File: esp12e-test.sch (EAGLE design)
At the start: 15 parts, among them IC1 ESP-12E/F, U8 NCP1117LPST50T3G

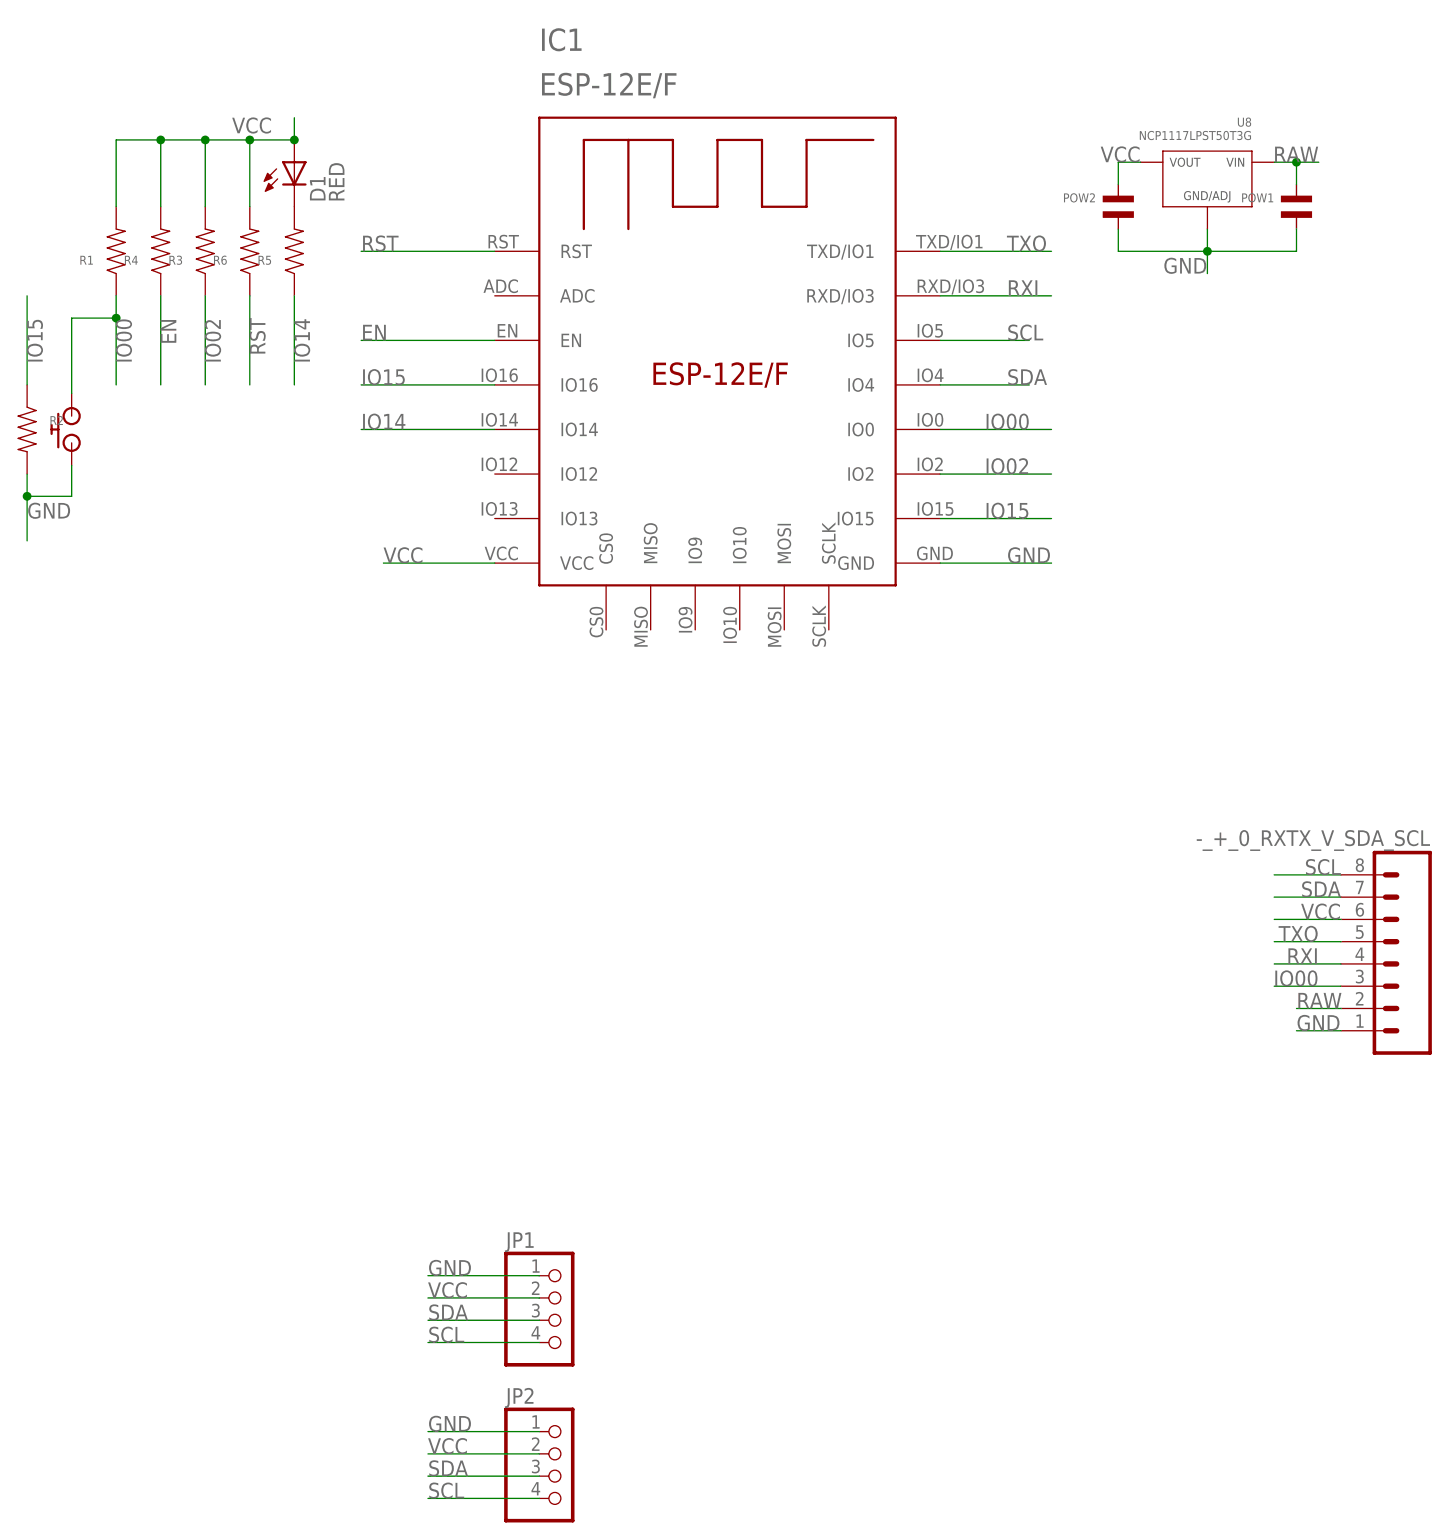
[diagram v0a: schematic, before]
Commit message: Fix IO16 bug, change to better stemma-st connector
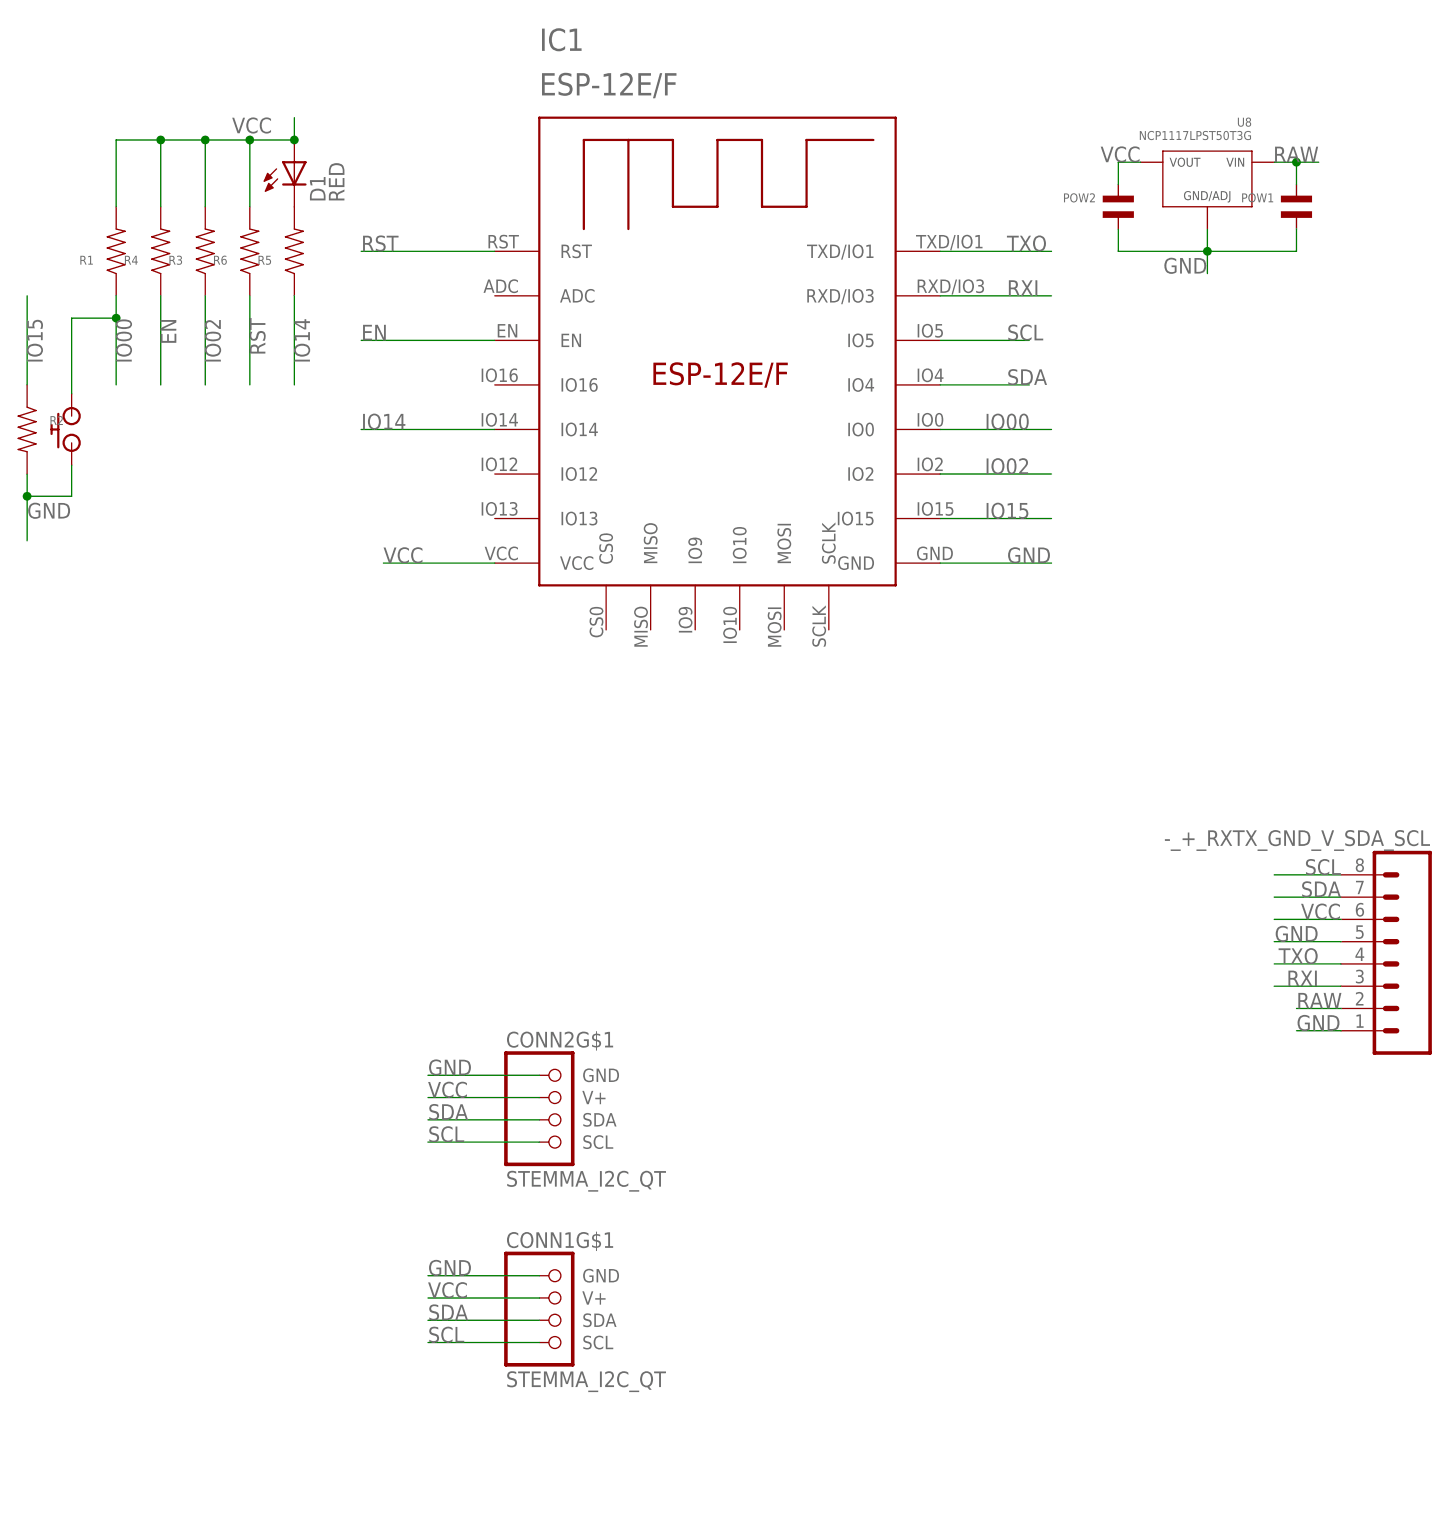
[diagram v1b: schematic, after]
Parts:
- removed JP1, JP2: (no value), microbuilder:HEADER-1X41MMPADS
- added CONN1, CONN2: STEMMA_I2C_QT, 00jim:STEMMA_I2C_QT
- renumbered -_+_0_RXTX_V_SDA_SCL to -_+_RXTX_GND_V_SDA_SCL
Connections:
- net GND: now also -_+_RXTX_GND_V_SDA_SCL.5, CONN1G$1.GND, CONN2G$1.GND; no longer JP1.1, JP2.1
- net IO00: no longer -_+_RXTX_GND_V_SDA_SCL.3
- net IO15: no longer IC1.IO16
- net RXI: now also -_+_RXTX_GND_V_SDA_SCL.3; no longer -_+_RXTX_GND_V_SDA_SCL.4
- net SCL: now also CONN1G$1.SCL, CONN2G$1.SCL; no longer JP1.4, JP2.4
- net SDA: now also CONN1G$1.SDA, CONN2G$1.SDA; no longer JP1.3, JP2.3
- net TXO: now also -_+_RXTX_GND_V_SDA_SCL.4; no longer -_+_RXTX_GND_V_SDA_SCL.5
- net VCC: now also CONN1G$1.V+, CONN2G$1.V+; no longer JP1.2, JP2.2
